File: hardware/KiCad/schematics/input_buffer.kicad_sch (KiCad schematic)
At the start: 12 parts, among them U2 MCP6022

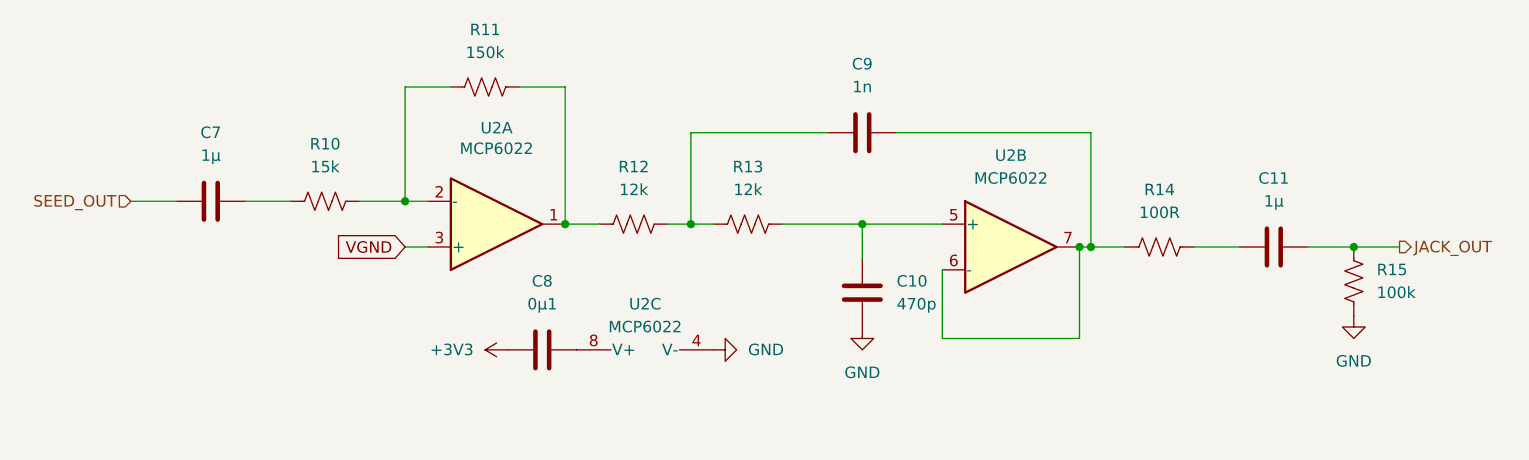
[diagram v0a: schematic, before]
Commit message: Footprint assignments for most components; file organization.
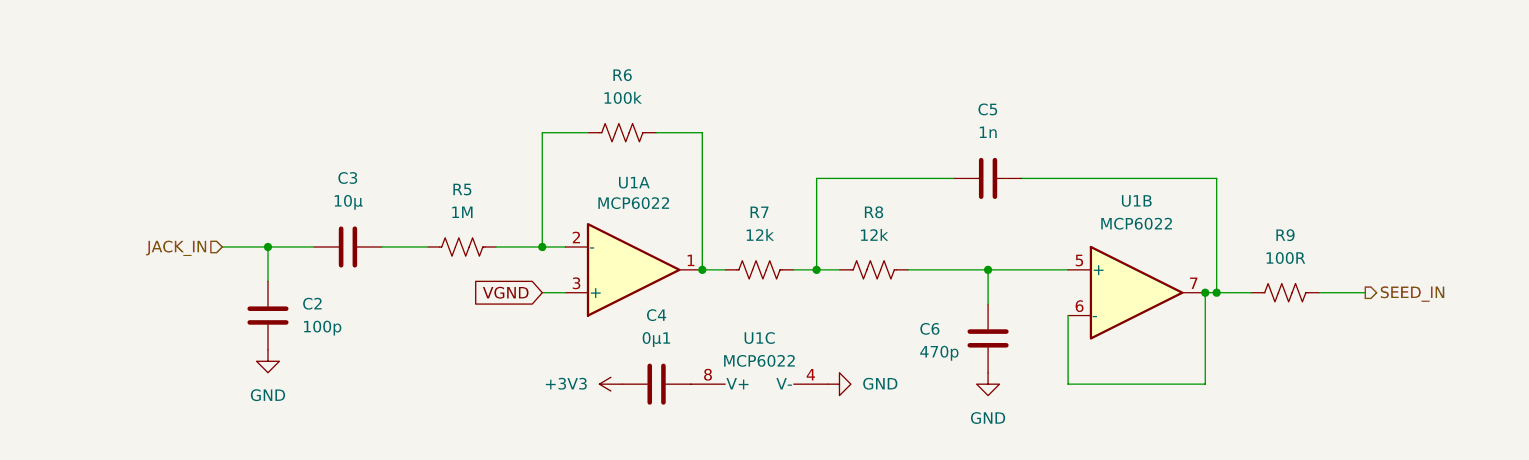
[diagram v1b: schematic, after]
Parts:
- removed C10: 470p, symbol Device:C
- removed C11, C7: 1µ, symbol Device:C
- removed C8: 0µ1, symbol Device:C
- removed C9: 1n, symbol Device:C
- removed R10: 15k, symbol Device:R_US
- removed R11: 150k, symbol Device:R_US
- removed R12, R13: 12k, symbol Device:R_US
- removed R14: 100R, symbol Device:R_US
- removed R15: 100k, symbol Device:R_US
- removed U2: MCP6022, symbol Amplifier_Operational:MCP6022
- added C2: 100p, Capacitor_THT:C_Rect_L4.0mm_W2.5mm_P2.50mm, symbol Device:C
- added C3: 10µ, Capacitor_THT:C_Rect_L7.0mm_W2.5mm_P5.00mm, symbol Device:C
- added C4: 0µ1, Capacitor_THT_Custom:C_Rect_L4.0mm_W2.6mm_P2.50mm, symbol Device:C
- added C5: 1n, Capacitor_THT:C_Rect_L4.0mm_W2.5mm_P2.50mm, symbol Device:C
- added C6: 470p, Capacitor_THT:C_Rect_L4.0mm_W2.5mm_P2.50mm, symbol Device:C
- added R5: 1M, Resistor_THT:R_Axial_DIN0207_L6.3mm_D2.5mm_P7.62mm_Horizontal, symbol Device:R_US
- added R6: 100k, Resistor_THT:R_Axial_DIN0207_L6.3mm_D2.5mm_P7.62mm_Horizontal, symbol Device:R_US
- added R7, R8: 12k, Resistor_THT:R_Axial_DIN0207_L6.3mm_D2.5mm_P7.62mm_Horizontal, symbol Device:R_US
- added R9: 100R, Resistor_THT:R_Axial_DIN0207_L6.3mm_D2.5mm_P7.62mm_Horizontal, symbol Device:R_US
- added U1: MCP6022, Package_DIP:DIP-8_W7.62mm, symbol Amplifier_Operational:MCP6022
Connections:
- net +3V3: now also C4.1
- net GND: now also C2.2, C6.2, U1.4 (V-)
- net VGND: now also U1.3 (+)
- new net: C5.1, R7.2, R8.1
- new net: C5.2, R9.1, U1.6 (-), U1.7
- new net: C6.1, R8.2, U1.5 (+)
- new net: R6.2, R7.1, U1.1
- new net: C3.1, R5.1
- new net: R5.2, R6.1, U1.2 (-)
- new net: C4.2, U1.8 (V+)
- new net JACK_IN: C2.1, C3.2
- new net SEED_IN: R9.2

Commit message: Added power flags.
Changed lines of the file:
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@@
+	)
+	(junction
+		(at 137.16 115.57)
+		(diameter 0)
+		(color 0 0 0 0)
 	)
 	(junction
@@
 					(unit 1)
 				)
+			)
+		)
+	)
+	(symbol
+		(lib_id "power:PWR_FLAG")
+		(at 137.16 115.57 180)
+		(unit 1)
+		(body_style 1)
+		(exclude_from_sim no)
+		(in_bom yes)
+		(on_board yes)
+		(in_pos_files yes)
+		(dnp no)
+		(fields_autoplaced yes)
+		(property "Reference" "#FLG04"
+			(at 137.16 117.475 0)
+			(hide yes)
+			(show_name no)
+			(do_not_autoplace no)
+			(effects
+				(font
+					(size 1.27 1.27)
+				)
+			)
+		)
+		(property "Value" "PWR_FLAG"
+			(at 137.16 120.65 0)
+			(show_name no)
+			(do_not_autoplace no)
+			(effects
+				(font
+					(size 1.27 1.27)
+				)
+			)
+		)
+		(property "Footprint" ""
+			(at 137.16 115.57 0)
+			(hide yes)
+			(show_name no)
+			(do_not_autoplace no)
+			(effects
+				(font
+					(size 1.27 1.27)
+				)
+			)
+		)
+		(property "Datasheet" ""
+			(at 137.16 115.57 0)
+			(hide yes)
+			(show_name no)
+			(do_not_autoplace no)
+			(effects
+				(font
+					(size 1.27 1.27)
+				)
+			)
+		)
+		(property "Description" "Special symbol for telling ERC where power comes from"
+			(at 137.16 115.57 0)
+			(hide yes)
+			(show_name no)
+			(do_not_autoplace no)
+			(effects
+				(font
+					(size 1.27 1.27)
+				)
+			)
+		)
+		(pin "1"
+		)
+		(instances
+			(project "freq-fiche"
+				(path "/fc444d3c-3a1a-4715-bcff-119f4d2b4d9e/5a5a17f9-5733-4e29-97e0-85beffe17bcf"
+					(reference "#FLG04")
+					(unit 1)
+				)

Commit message: Power conditioning.
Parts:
- C4: value 0µ1 -> 100n
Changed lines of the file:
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@@
 			)
 		)
-		(property "Value" "0µ1"
+		(property "Value" "100n"
 			(at 133.35 110.49 90)
 			(show_name no)

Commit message: Gain staging; source pin reassignments.
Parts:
- R6: value 100k -> 1M5
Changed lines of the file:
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@@
 			)
 		)
-		(property "Value" "100k"
+		(property "Value" "1M5"
 			(at 129.54 83.82 90)
 			(show_name no)
